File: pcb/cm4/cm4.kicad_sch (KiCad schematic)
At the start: 4 parts, among them J101 Conn_02x10_Row_Letter_First

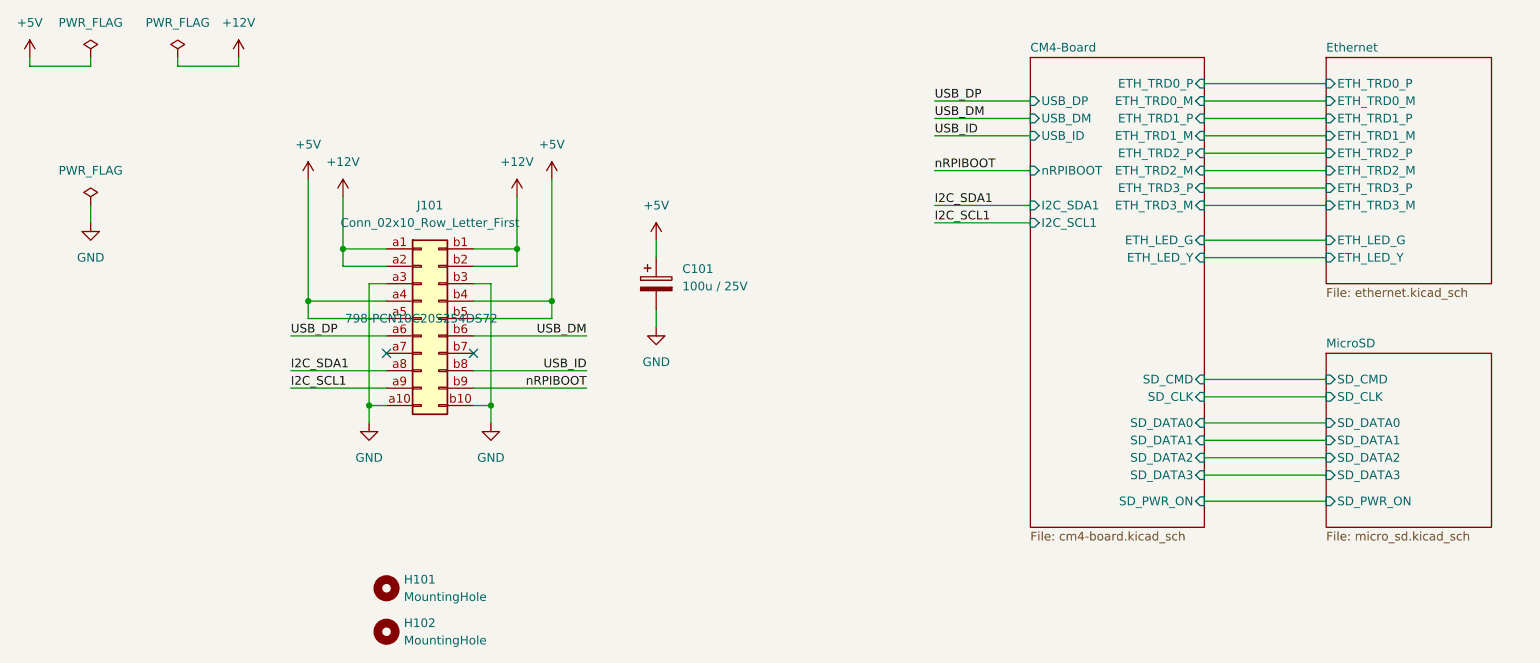
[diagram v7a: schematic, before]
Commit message: rename differential nets correctly and fix cm4 footprint
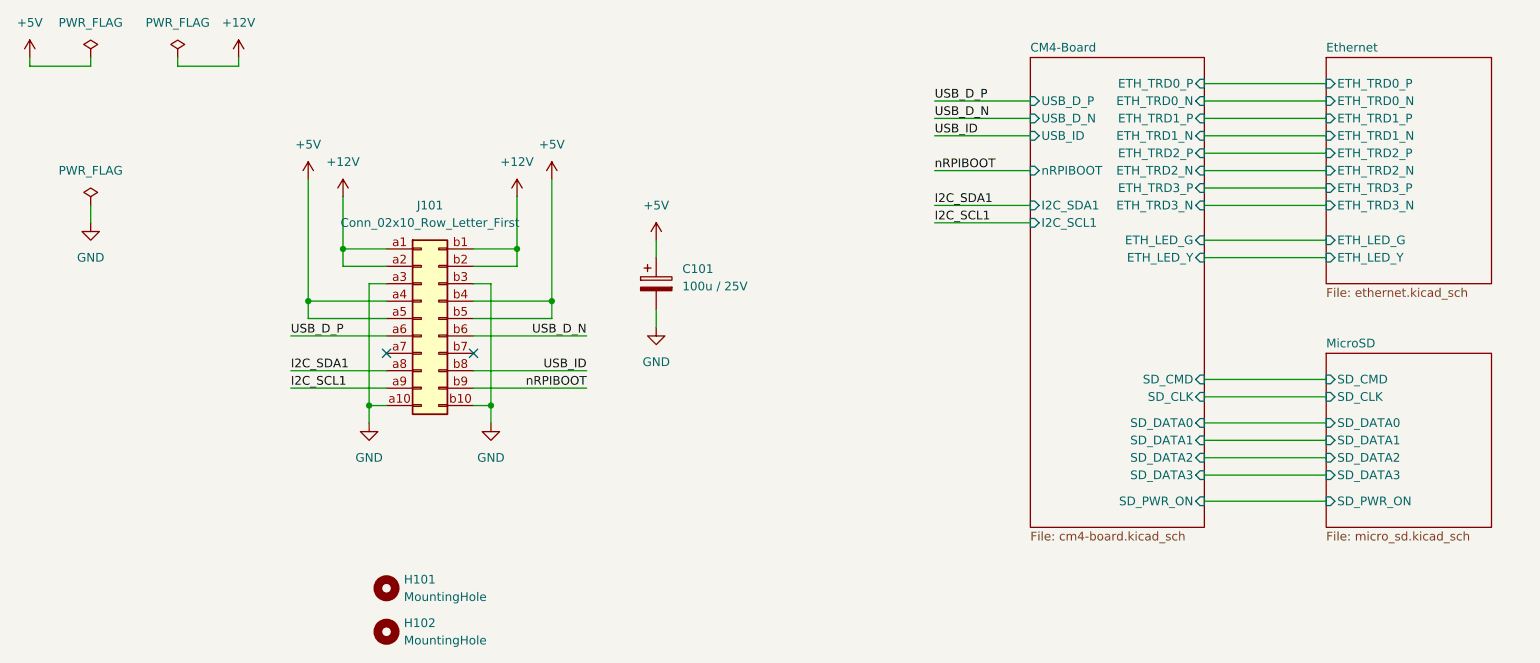
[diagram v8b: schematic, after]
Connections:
- net USB_DM renamed USB_D_N
- net USB_DP renamed USB_D_P
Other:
- sheet CM4-Board ports: added ETH_TRD0_N, ETH_TRD1_N, ETH_TRD2_N, ETH_TRD3_N, USB_D_N, USB_D_P; removed ETH_TRD0_M, ETH_TRD1_M, ETH_TRD2_M, ETH_TRD3_M, USB_DM, USB_DP
- sheet Ethernet ports: added ETH_TRD0_N, ETH_TRD1_N, ETH_TRD2_N, ETH_TRD3_N; removed ETH_TRD0_M, ETH_TRD1_M, ETH_TRD2_M, ETH_TRD3_M
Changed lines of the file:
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@@
 		)
 	)
-	(label "USB_DP"
+	(label "USB_D_P"
 		(at 156.21 76.2 0)
 		(effects
@@
 		)
 	)
-	(label "USB_DP"
+	(label "USB_D_P"
 		(at 62.23 110.49 0)
 		(effects
@@
 		)
 	)
-	(label "USB_DM"
+	(label "USB_D_N"
 		(at 156.21 78.74 0)
 		(effects
@@
 		)
 	)
-	(label "USB_DM"
+	(label "USB_D_N"
 		(at 105.41 110.49 180)
 		(effects
@@
 					(size 1.27 1.27)
 				)
+				(hide yes)
 			)
 		)
@@
 			)
 		)
-		(pin "ETH_TRD0_M" input
-			(at 213.36 76.2 180)
-			(effects
-				(font
-					(size 1.27 1.27)
-				)
-				(justify left)
-			)
-		)
 		(pin "ETH_TRD0_P" input
 			(at 213.36 73.66 180)
@@
 			)
 		)
-		(pin "ETH_TRD1_M" input
-			(at 213.36 81.28 180)
-			(effects
-				(font
-					(size 1.27 1.27)
-				)
-				(justify left)
-			)
-		)
 		(pin "ETH_TRD1_P" input
 			(at 213.36 78.74 180)
@@
 			)
 		)
-		(pin "ETH_TRD2_M" input
-			(at 213.36 86.36 180)
-			(effects
-				(font
-					(size 1.27 1.27)
-				)
-				(justify left)
-			)
-		)
 		(pin "ETH_TRD2_P" input
 			(at 213.36 83.82 180)
@@
 			)
 		)
-		(pin "ETH_TRD3_M" input
-			(at 213.36 91.44 180)
-			(effects
-				(font
-					(size 1.27 1.27)
-				)
-				(justify left)
-			)
-		)
 		(pin "ETH_TRD3_P" input
 			(at 213.36 88.9 180)
+			(effects
+				(font
+					(size 1.27 1.27)
+				)
+				(justify left)
+			)
+		)
+		(pin "ETH_TRD0_N" input
+			(at 213.36 76.2 180)
+			(effects
+				(font
+					(size 1.27 1.27)
+				)
+				(justify left)
+			)
+		)
+		(pin "ETH_TRD1_N" input
+			(at 213.36 81.28 180)
+			(effects
+				(font
+					(size 1.27 1.27)
+				)
+				(justify left)
+			)
+		)
+		(pin "ETH_TRD2_N" input
+			(at 213.36 86.36 180)
+			(effects
+				(font
+					(size 1.27 1.27)
+				)
+				(justify left)
+			)
+		)
+		(pin "ETH_TRD3_N" input
+			(at 213.36 91.44 180)
 			(effects
 				(font
@@
 			)
 		)
-		(pin "ETH_TRD0_M" input
-			(at 195.58 76.2 0)
-			(effects
-				(font
-					(size 1.27 1.27)
-				)
-				(justify right)
-			)
-		)
 		(pin "ETH_TRD0_P" input
 			(at 195.58 73.66 0)
@@
 			)
 		)
-		(pin "ETH_TRD1_M" input
-			(at 195.58 81.28 0)
-			(effects
-				(font
-					(size 1.27 1.27)
-				)
-				(justify right)
-			)
-		)
 		(pin "ETH_TRD1_P" input
 			(at 195.58 78.74 0)
@@
 			)
 		)
-		(pin "ETH_TRD2_M" input
-			(at 195.58 86.36 0)
-			(effects
-				(font
-					(size 1.27 1.27)
-				)
-				(justify right)
-			)
-		)
 		(pin "ETH_TRD2_P" input
 			(at 195.58 83.82 0)
@@
 			)
 		)
-		(pin "ETH_TRD3_M" input
-			(at 195.58 91.44 0)
-			(effects
-				(font
-					(size 1.27 1.27)
-				)
-				(justify right)
-			)
-		)
 		(pin "ETH_TRD3_P" input
 			(at 195.58 88.9 0)
@@
 			)
 		)
-		(pin "USB_DM" input
-			(at 170.18 78.74 180)
-			(effects
-				(font
-					(size 1.27 1.27)
-				)
-				(justify left)
-			)
-		)
-		(pin "USB_DP" input
-			(at 170.18 76.2 180)
-			(effects
-				(font
-					(size 1.27 1.27)
-				)
-				(justify left)
-			)
-		)
 		(pin "USB_ID" input
 			(at 170.18 81.28 180)
 			(effects
 				(font
+					(size 1.27 1.27)
+				)
+				(justify left)
+			)
+		)
+		(pin "ETH_TRD0_N" input
+			(at 195.58 76.2 0)
+			(effects
+				(font
+					(size 1.27 1.27)
+				)
+				(justify right)
+			)
+		)
+		(pin "ETH_TRD1_N" input
+			(at 195.58 81.28 0)
+			(effects
+				(font
+					(size 1.27 1.27)
+				)
+				(justify right)
+			)
+		)
+		(pin "ETH_TRD2_N" input
+			(at 195.58 86.36 0)
+			(effects
+				(font
+					(size 1.27 1.27)
+				)
+				(justify right)
+			)
+		)
+		(pin "ETH_TRD3_N" input
+			(at 195.58 91.44 0)
+			(effects
+				(font
+					(size 1.27 1.27)
+				)
+				(justify right)
+			)
+		)
+		(pin "USB_D_N" input
+			(at 170.18 78.74 180)
+			(effects
+				(font
+					(size 1.27 1.27)
+				)
+				(justify left)
+			)
+		)
+		(pin "USB_D_P" input
+			(at 170.18 76.2 180)
+			(effects
+				(font
